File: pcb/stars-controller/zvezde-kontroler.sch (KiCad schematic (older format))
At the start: 28 parts, among them IC1 ATTINY841-SSU, J1 TLC5925, J10 RJ45, J11 RJ45, J12 RJ45, J2 TLC5925, J3 RJ45, J4 RJ45, J5 RJ45, J6 RJ45, J7 RJ45, J8 RJ45, J9 RJ45, P1 CONN_01X08, P2 CONN_01X08, P3 CONN_01X06, P4 CONN_01X08, P5 CONN_01X04, P6 CONN_01X08, P7 CONN_01X04

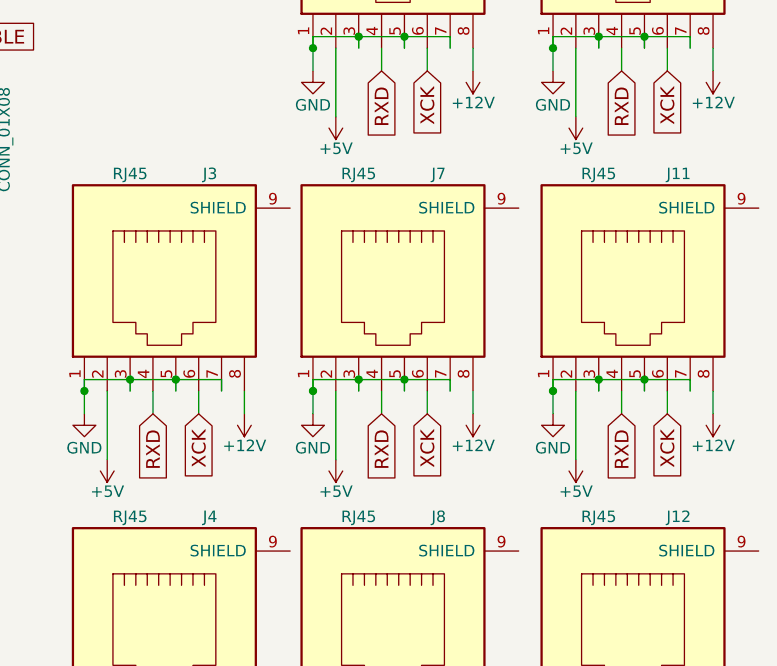
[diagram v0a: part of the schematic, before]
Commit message: Double sided pcbs
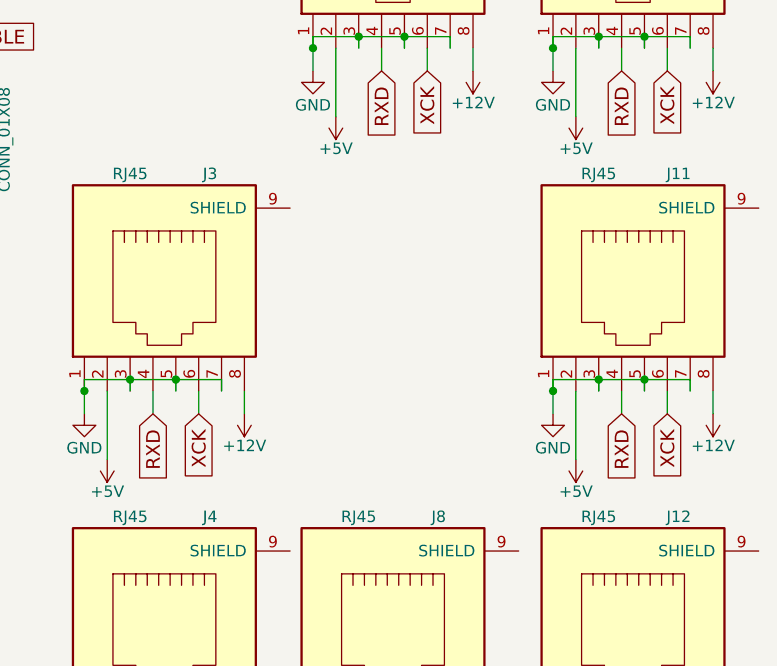
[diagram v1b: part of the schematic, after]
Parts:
- removed J7: RJ45, rj45:RJ45, symbol RJ45
- P3: footprint attiny841-spi:ATTINY841-SPI -> Pin_Headers:Pin_Header_Straight_2x03_Pitch2.54mm
